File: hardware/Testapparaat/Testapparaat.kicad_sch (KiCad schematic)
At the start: 29 parts, among them J1 IO_SD, J14 GPIO_OUTPUT, J2 Module_1, J3 Module_2, J6 IO_UART, J7 Emergency Stop Button, Q3 BC817, Q4 IRFR9024N, Q5 IRFR9024N, Q6 IRFR9024N, U1 74HC595 (SIPO Shift register), U3 74AHC1G02, U4 74HC595 (SIPO Shift register), U5 TCA9534 (IO Expander), U6 74HC14, U7 TCA9534 (IO Expander)

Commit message: -enh Made a start at pcb design
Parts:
- removed D9: 1N4448, Diode_THT:D_DO-35_SOD27_P7.62mm_Horizontal, symbol Diode:1N4448
- removed U3: 74AHC1G02, 74AHC1G02:SOTFL50P160X60-5N, symbol 74xGxx:74AHC1G02
- added D3: 1N4448WS, Diode_SMD:D_SOD-323, symbol Diode:1N4448WS
- added R36, R37: 100k, Resistor_SMD:R_0603_1608Metric_Pad0.98x0.95mm_HandSolder, symbol Device:R
- added R38, R40, R41: 10k, Resistor_SMD:R_0603_1608Metric_Pad0.98x0.95mm_HandSolder, symbol Device:R_Small
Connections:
- net +3.3V: now also R38.2, R40.2, R41.2; no longer C14.2, C15.2, C16.2, C17.2, C21.2, J1.6 (Pin_6), J2.1 (Pin_1), J2.9 (Pin_9), J3.1 (Pin_1), J3.9 (Pin_9), J6.4 (Pin_4), J7.1, Q3.2 (E), R32.2, U1.8 (GND), U4.8 (GND), U5.1 (A0), U5.2 (A1), U5.3 (A2), U5.8 (GND), U7.1 (A0), U7.2 (A1), U7.3 (A2), U7.8 (GND)
- net EMERGENCY_STOP_BTN: now also D3.2 (A)
- net I2C_SCL: now also R40.1
- net I2C_SDA: now also R38.1
- net ID_MOD_1: now also R37.2
- net ID_MOD_2: now also R36.2
- net IO_EXP_INT: now also U5.13 (~{INT}), U7.13 (~{INT}), R41.1
- net at C21.1, R33.2, U6.1: now also D3.1 (K)
- new net GND: C14.2, C15.2, C16.2, C17.2, C21.2, J1.6 (Pin_6), J2.1 (Pin_1), J2.9 (Pin_9), J3.1 (Pin_1), J3.9 (Pin_9), J6.4 (Pin_4), J7.1, Q3.2 (E), R32.2, U1.8 (GND), U4.8 (GND), U5.1 (A0), U5.2 (A1), U5.3 (A2), U5.8 (GND), U7.1 (A0), U7.2 (A1), U7.3 (A2), U7.8 (GND)
- new net MCU/SENSOR_VN/GPIO_IN_39: R36.1
- new net MCU/SENSOR_VP/GPIO_IN_36: R37.1
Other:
- sheet Power Supply ports: added none; removed 3.3V_OUT, 5V_OUT, BATT_OUT+, BATT_OUT-

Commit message: -enh change slave address of second io expander
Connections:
- net +3.3V: now also U7.1 (A0)
- net GND: no longer U7.1 (A0)
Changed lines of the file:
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@@
   (junction (at 155.448 156.972) (diameter 0) (color 0 0 0 0)
-  )
-  (junction (at 245.11 67.056) (diameter 0) (color 0 0 0 0)
   )
   (junction (at 255.27 39.37) (diameter 0) (color 0 0 0 0)
@@
     (stroke (width 0) (type default) (color 0 0 0 0))
   )
-  (wire (pts (xy 245.11 64.516) (xy 245.11 67.056))
-    (stroke (width 0) (type default) (color 0 0 0 0))
-  )
   (wire (pts (xy 56.515 58.42) (xy 56.515 62.611))
     (stroke (width 0) (type default) (color 0 0 0 0))
@@
     (pin "8")
   )
+  (symbol (lib_id "power:+3.3V") (at 245.11 64.516 0) (unit 1)
+    (in_bom yes) (on_board yes)
+    (property "Reference" "#PWR?" (id 0) (at 245.11 68.326 0)
+      (effects (font (size 1.27 1.27)) hide)
+    )
+    (property "Value" "+3.3V" (id 1) (at 245.11 60.706 0))
+    (property "Footprint" "" (id 2) (at 245.11 64.516 0)
+      (effects (font (size 1.27 1.27)) hide)
+    )
+    (property "Datasheet" "" (id 3) (at 245.11 64.516 0)
+      (effects (font (size 1.27 1.27)) hide)
+    )
+    (pin "1")
+  )
   (symbol (lib_id "Device:C_Small") (at 217.17 22.352 0) (unit 1)
     (in_bom yes) (on_board yes)
@@
       (reference "#PWR0122") (unit 1) (value "+5V") (footprint "")
     )
+    (path "/a2b2e4c3-2b40-402e-8bd9-3aec2f8c5db0"
+      (reference "#PWR?") (unit 1) (value "+3.3V") (footprint "")
+    )
     (path "/2a1f4b25-2db4-4c7f-ba5e-95c06f30cc5e/e59693f2-1c09-4e8e-9ae0-141b8d24c586"

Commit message: -enh more routing
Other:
- note added: "Series resistor gate"
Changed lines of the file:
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@@
     (effects (font (size 3 3)) (justify left bottom))
+  )
+  (text "Series resistor gate" (at 107.188 187.198 0)
+    (effects (font (size 1.27 1.27)) (justify left bottom))
   )
   (text "GPIO Expanders / Shift registers" (at 199.136 17.78 0)

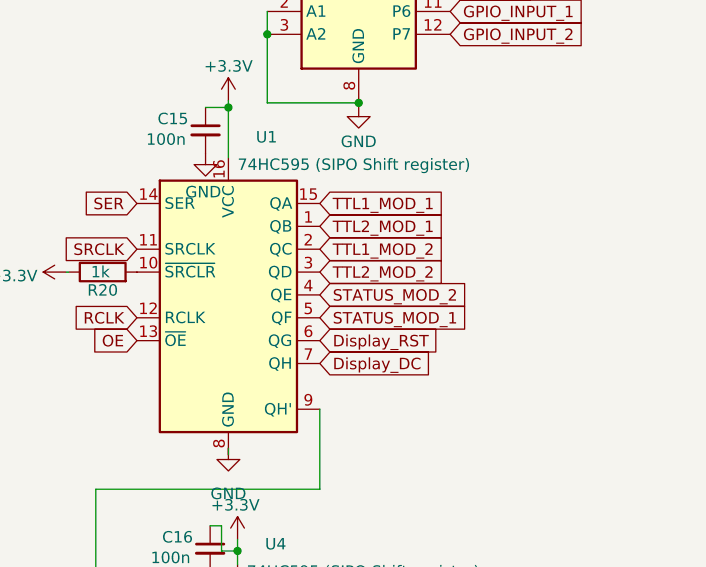
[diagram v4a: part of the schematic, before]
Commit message: -enh Routed most of the module sections
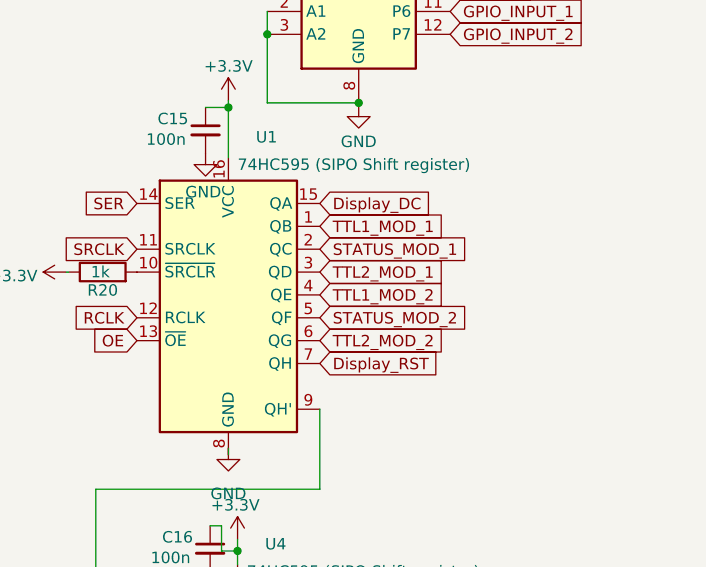
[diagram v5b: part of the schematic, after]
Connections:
- net Display_DC: now also U1.15 (QA); no longer U1.7 (QH)
- net Display_RST: now also U1.7 (QH); no longer U1.6 (QG)
- net STATUS_MOD_1: now also U1.2 (QC); no longer U1.5 (QF)
- net STATUS_MOD_2: now also U1.5 (QF); no longer U1.4 (QE)
- net TTL1_MOD_1: now also U1.1 (QB); no longer U1.15 (QA)
- net TTL1_MOD_2: now also U1.4 (QE); no longer U1.2 (QC)
- net TTL2_MOD_1: now also U1.3 (QD); no longer U1.1 (QB)
- net TTL2_MOD_2: now also U1.6 (QG); no longer U1.3 (QD)
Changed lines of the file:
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@@
     )
   )
-  (global_label "Display_DC" (shape input) (at 250.952 106.172 0) (fields_autoplaced)
-    (effects (font (size 1.27 1.27)) (justify left))
-    (property "Intersheet-verwijzingen" "${INTERSHEET_REFS}" (id 0) (at 263.7065 106.0926 0)
+  (global_label "Display_DC" (shape input) (at 250.952 88.392 0) (fields_autoplaced)
+    (effects (font (size 1.27 1.27)) (justify left))
+    (property "Intersheet-verwijzingen" "${INTERSHEET_REFS}" (id 0) (at 263.7065 88.3126 0)
       (effects (font (size 1.27 1.27)) (justify left) hide)
     )
@@
     )
   )
-  (global_label "TTL1_MOD_2" (shape input) (at 250.952 93.472 0) (fields_autoplaced)
-    (effects (font (size 1.27 1.27)) (justify left))
-    (property "Intersheet-verwijzingen" "${INTERSHEET_REFS}" (id 0) (at 264.7346 93.3926 0)
+  (global_label "TTL1_MOD_2" (shape input) (at 250.952 98.552 0) (fields_autoplaced)
+    (effects (font (size 1.27 1.27)) (justify left))
+    (property "Intersheet-verwijzingen" "${INTERSHEET_REFS}" (id 0) (at 264.7346 98.4726 0)
       (effects (font (size 1.27 1.27)) (justify left) hide)
     )
@@
     )
   )
-  (global_label "TTL2_MOD_2" (shape input) (at 250.952 96.012 0) (fields_autoplaced)
-    (effects (font (size 1.27 1.27)) (justify left))
-    (property "Intersheet-verwijzingen" "${INTERSHEET_REFS}" (id 0) (at 264.7346 95.9326 0)
+  (global_label "TTL2_MOD_2" (shape input) (at 250.952 103.632 0) (fields_autoplaced)
+    (effects (font (size 1.27 1.27)) (justify left))
+    (property "Intersheet-verwijzingen" "${INTERSHEET_REFS}" (id 0) (at 264.7346 103.5526 0)
       (effects (font (size 1.27 1.27)) (justify left) hide)
     )
@@
     )
   )
-  (global_label "TTL1_MOD_1" (shape input) (at 250.952 88.392 0) (fields_autoplaced)
-    (effects (font (size 1.27 1.27)) (justify left))
-    (property "Intersheet-verwijzingen" "${INTERSHEET_REFS}" (id 0) (at 264.7346 88.4714 0)
+  (global_label "TTL1_MOD_1" (shape input) (at 250.952 90.932 0) (fields_autoplaced)
+    (effects (font (size 1.27 1.27)) (justify left))
+    (property "Intersheet-verwijzingen" "${INTERSHEET_REFS}" (id 0) (at 264.7346 91.0114 0)
       (effects (font (size 1.27 1.27)) (justify left) hide)
     )
@@
     )
   )
-  (global_label "STATUS_MOD_2" (shape input) (at 250.952 98.552 0) (fields_autoplaced)
-    (effects (font (size 1.27 1.27)) (justify left))
-    (property "Intersheet-verwijzingen" "${INTERSHEET_REFS}" (id 0) (at 267.3351 98.4726 0)
+  (global_label "STATUS_MOD_2" (shape input) (at 250.952 101.092 0) (fields_autoplaced)
+    (effects (font (size 1.27 1.27)) (justify left))
+    (property "Intersheet-verwijzingen" "${INTERSHEET_REFS}" (id 0) (at 267.3351 101.0126 0)
       (effects (font (size 1.27 1.27)) (justify left) hide)
     )
@@
     )
   )
-  (global_label "STATUS_MOD_1" (shape input) (at 250.952 101.092 0) (fields_autoplaced)
-    (effects (font (size 1.27 1.27)) (justify left))
-    (property "Intersheet-verwijzingen" "${INTERSHEET_REFS}" (id 0) (at 267.3351 101.0126 0)
-      (effects (font (size 1.27 1.27)) (justify left) hide)
-    )
-  )
-  (global_label "TTL2_MOD_1" (shape input) (at 250.952 90.932 0) (fields_autoplaced)
-    (effects (font (size 1.27 1.27)) (justify left))
-    (property "Intersheet-verwijzingen" "${INTERSHEET_REFS}" (id 0) (at 264.7346 91.0114 0)
+  (global_label "STATUS_MOD_1" (shape input) (at 250.952 93.472 0) (fields_autoplaced)
+    (effects (font (size 1.27 1.27)) (justify left))
+    (property "Intersheet-verwijzingen" "${INTERSHEET_REFS}" (id 0) (at 267.3351 93.3926 0)
+      (effects (font (size 1.27 1.27)) (justify left) hide)
+    )
+  )
+  (global_label "TTL2_MOD_1" (shape input) (at 250.952 96.012 0) (fields_autoplaced)
+    (effects (font (size 1.27 1.27)) (justify left))
+    (property "Intersheet-verwijzingen" "${INTERSHEET_REFS}" (id 0) (at 264.7346 96.0914 0)
       (effects (font (size 1.27 1.27)) (justify left) hide)
     )
@@
     )
   )
-  (global_label "Display_RST" (shape input) (at 250.952 103.632 0) (fields_autoplaced)
-    (effects (font (size 1.27 1.27)) (justify left))
-    (property "Intersheet-verwijzingen" "${INTERSHEET_REFS}" (id 0) (at 264.6137 103.7114 0)
+  (global_label "Display_RST" (shape input) (at 250.952 106.172 0) (fields_autoplaced)
+    (effects (font (size 1.27 1.27)) (justify left))
+    (property "Intersheet-verwijzingen" "${INTERSHEET_REFS}" (id 0) (at 264.6137 106.2514 0)
       (effects (font (size 1.27 1.27)) (justify left) hide)
     )
@@
   (symbol (lib_id "power:+3.3V") (at 245.11 64.516 0) (unit 1)
     (in_bom yes) (on_board yes)
-    (property "Reference" "#PWR?" (id 0) (at 245.11 68.326 0)
+    (property "Reference" "#PWR0123" (id 0) (at 245.11 68.326 0)
       (effects (font (size 1.27 1.27)) hide)
     )
@@
     )
     (path "/a2b2e4c3-2b40-402e-8bd9-3aec2f8c5db0"
-      (reference "#PWR?") (unit 1) (value "+3.3V") (footprint "")
+      (reference "#PWR0123") (unit 1) (value "+3.3V") (footprint "")
     )
     (path "/2a1f4b25-2db4-4c7f-ba5e-95c06f30cc5e/e59693f2-1c09-4e8e-9ae0-141b8d24c586"

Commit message: -enh more routing
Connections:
- net EMERGENCY_STOP_BTN: now also U5.4 (P0); no longer U5.6 (P2)
- net Rotary_BTN: now also U5.5 (P1); no longer U5.7 (P3)
- net TTL3_MOD_1: now also U5.6 (P2); no longer U5.4 (P0)
- net TTL3_MOD_2: now also U5.7 (P3); no longer U5.5 (P1)
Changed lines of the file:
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@@
     )
   )
-  (global_label "EMERGENCY_STOP_BTN" (shape input) (at 230.124 35.56 0) (fields_autoplaced)
+  (global_label "EMERGENCY_STOP_BTN" (shape input) (at 230.124 30.48 0) (fields_autoplaced)
     (effects (font (size 1.27 1.27)) (justify left))
-    (property "Intersheet-verwijzingen" "${INTERSHEET_REFS}" (id 0) (at 253.9457 35.6394 0)
+    (property "Intersheet-verwijzingen" "${INTERSHEET_REFS}" (id 0) (at 253.9457 30.5594 0)
       (effects (font (size 1.27 1.27)) (justify left) hide)
     )
@@
     )
   )
-  (global_label "TTL3_MOD_2" (shape input) (at 230.124 33.02 0) (fields_autoplaced)
+  (global_label "TTL3_MOD_2" (shape input) (at 230.124 38.1 0) (fields_autoplaced)
     (effects (font (size 1.27 1.27)) (justify left))
-    (property "Intersheet-verwijzingen" "${INTERSHEET_REFS}" (id 0) (at 243.9066 32.9406 0)
+    (property "Intersheet-verwijzingen" "${INTERSHEET_REFS}" (id 0) (at 243.9066 38.0206 0)
       (effects (font (size 1.27 1.27)) (justify left) hide)
     )
@@
     )
   )
-  (global_label "Rotary_BTN" (shape input) (at 230.124 38.1 0) (fields_autoplaced)
+  (global_label "Rotary_BTN" (shape input) (at 230.124 33.02 0) (fields_autoplaced)
     (effects (font (size 1.27 1.27)) (justify left))
-    (property "Intersheet-verwijzingen" "${INTERSHEET_REFS}" (id 0) (at 243.1204 38.1794 0)
+    (property "Intersheet-verwijzingen" "${INTERSHEET_REFS}" (id 0) (at 243.1204 33.0994 0)
       (effects (font (size 1.27 1.27)) (justify left) hide)
     )
@@
     )
   )
-  (global_label "TTL3_MOD_1" (shape input) (at 230.124 30.48 0) (fields_autoplaced)
+  (global_label "TTL3_MOD_1" (shape input) (at 230.124 35.56 0) (fields_autoplaced)
     (effects (font (size 1.27 1.27)) (justify left))
-    (property "Intersheet-verwijzingen" "${INTERSHEET_REFS}" (id 0) (at 243.9066 30.4006 0)
+    (property "Intersheet-verwijzingen" "${INTERSHEET_REFS}" (id 0) (at 243.9066 35.4806 0)
       (effects (font (size 1.27 1.27)) (justify left) hide)
     )

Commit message: -add gerbers and minor improvements
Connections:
- net GPIO_INPUT_2 renamed Display_TP_CS
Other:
- sheet Display ports: added Display_TP_CS; removed none
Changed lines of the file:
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@@
+    (stroke (width 0) (type default) (color 0 0 0 0))
+  )
+  (wire (pts (xy 57.15 66.548) (xy 77.724 66.548))
     (stroke (width 0) (type default) (color 0 0 0 0))
   )
@@
     (stroke (width 0) (type default) (color 0 0 0 0))
   )
+  (wire (pts (xy 57.15 60.706) (xy 57.15 66.548))
+    (stroke (width 0) (type default) (color 0 0 0 0))
+  )
   (wire (pts (xy 106.934 154.94) (xy 106.934 155.956))
     (stroke (width 0) (type default) (color 0 0 0 0))
@@
     (stroke (width 0) (type default) (color 0 0 0 0))
   )
+  (wire (pts (xy 77.724 61.722) (xy 78.486 61.722))
+    (stroke (width 0) (type default) (color 0 0 0 0))
+  )
   (wire (pts (xy 240.792 76.962) (xy 240.792 77.724))
     (stroke (width 0) (type default) (color 0 0 0 0))
@@
     (stroke (width 0) (type default) (color 0 0 0 0))
   )
+  (wire (pts (xy 77.724 66.548) (xy 77.724 61.722))
+    (stroke (width 0) (type default) (color 0 0 0 0))
+  )
   (wire (pts (xy 147.32 188.214) (xy 155.448 188.214))
     (stroke (width 0) (type default) (color 0 0 0 0))
@@
   )
   (wire (pts (xy 53.975 48.26) (xy 57.785 48.26))
+    (stroke (width 0) (type default) (color 0 0 0 0))
+  )
+  (wire (pts (xy 57.15 60.706) (xy 57.785 60.706))
     (stroke (width 0) (type default) (color 0 0 0 0))
   )
@@
     )
   )
-  (global_label "GPIO_INPUT_2" (shape input) (at 265.43 69.596 0) (fields_autoplaced)
-    (effects (font (size 1.27 1.27)) (justify left))
-    (property "Intersheet-verwijzingen" "${INTERSHEET_REFS}" (id 0) (at 280.9664 69.5166 0)
-      (effects (font (size 1.27 1.27)) (justify left) hide)
-    )
-  )
   (global_label "STATUS_MOD_1" (shape input) (at 153.416 46.736 0) (fields_autoplaced)
     (effects (font (size 1.27 1.27)) (justify left))
@@
     )
   )
+  (global_label "Display_TP_CS" (shape output) (at 78.486 61.722 0) (fields_autoplaced)
+    (effects (font (size 1.27 1.27)) (justify left))
+    (property "Intersheet References" "${INTERSHEET_REFS}" (id 0) (at 94.3853 61.6426 0)
+      (effects (font (size 1.27 1.27)) (justify left) hide)
+    )
+  )
   (global_label "I2C_SDA" (shape input) (at 42.926 58.42 0) (fields_autoplaced)
     (effects (font (size 1.27 1.27)) (justify left))
@@
     (effects (font (size 1.27 1.27)) (justify left))
     (property "Intersheet-verwijzingen" "${INTERSHEET_REFS}" (id 0) (at 47.9517 73.5806 0)
+      (effects (font (size 1.27 1.27)) (justify left) hide)
+    )
+  )
+  (global_label "Display_TP_CS" (shape output) (at 265.43 69.596 0) (fields_autoplaced)
+    (effects (font (size 1.27 1.27)) (justify left))
+    (property "Intersheet References" "${INTERSHEET_REFS}" (id 0) (at 281.3293 69.5166 0)
       (effects (font (size 1.27 1.27)) (justify left) hide)
     )
@@
     )
   )
-  (sheet (at 57.785 44.45) (size 14.605 17.78) (fields_autoplaced)
+  (sheet (at 57.785 44.45) (size 15.875 18.288) (fields_autoplaced)
     (stroke (width 0.1524) (type solid) (color 0 0 0 0))
     (fill (color 0 0 0 0.0000))
@@
       (effects (font (size 1.27 1.27)) (justify left bottom))
     )
-    (property "Sheet file" "display.kicad_sch" (id 1) (at 57.785 62.8146 0)
+    (property "Sheet file" "display.kicad_sch" (id 1) (at 57.785 63.3226 0)
       (effects (font (size 1.27 1.27)) (justify left top))
     )
@@
       (effects (font (size 1.27 1.27)) (justify left))
     )
+    (pin "Display_TP_CS" input (at 57.785 60.706 180)
+      (effects (font (size 1.27 1.27)) (justify left))
+    )
